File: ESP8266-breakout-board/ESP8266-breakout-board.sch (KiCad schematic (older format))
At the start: 3 parts, among them J1 Conn_01x04_Male, J2 Conn_02x04_Top_Bottom, J3 Conn_01x04_Male

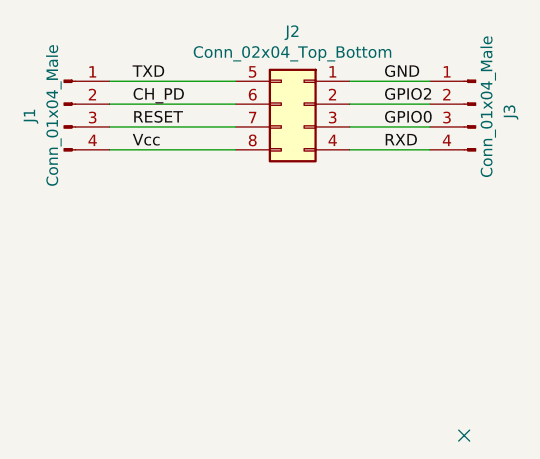
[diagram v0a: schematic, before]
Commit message: PCB esp8266-breakout-board
kicad-pcb with gerber files
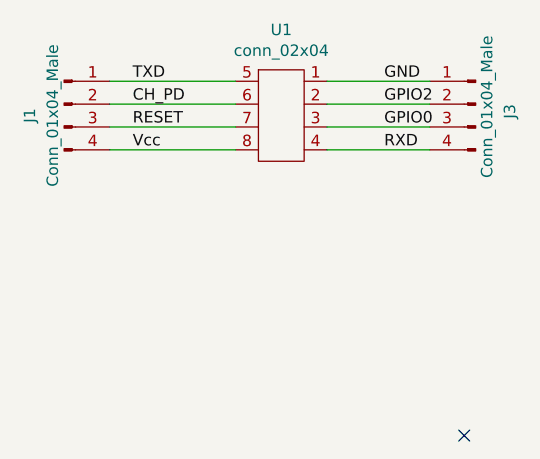
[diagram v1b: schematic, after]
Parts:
- removed J2: Conn_02x04_Top_Bottom, Connector_PinSocket_2.54mm:PinSocket_2x04_P2.54mm_Vertical, symbol Connector_Generic:Conn_02x04_Top_Bottom
- added U1: conn_02x04, conn_02x04:conn_02x04, symbol conn_02x04:conn_02x04
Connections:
- net CH_PD: now also U1.6
- net GND: now also U1.1
- net GPIO0: now also U1.3
- net GPIO2: now also U1.2
- net RESET: now also U1.7
- net RXD: now also U1.4
- net TXD: now also U1.5
- net Vcc: now also U1.8
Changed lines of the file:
@@
 NoConn ~ 5550 2550
 $Comp
-L Connector_Generic:Conn_02x04_Top_Bottom J2
-U 1 1 5F80BF5D
-P 4850 1100
-F 0 "J2" H 4900 1417 50  0000 C CNN
-F 1 "Conn_02x04_Top_Bottom" H 4900 1326 50  0000 C CNN
-F 2 "Connector_PinSocket_2.54mm:PinSocket_2x04_P2.54mm_Vertical" H 4850 1100 50  0001 C CNN
-F 3 "~" H 4850 1100 50  0001 C CNN
-	1    4850 1100
-	-1   0    0    -1
-$EndComp
-$Comp
 L Connector:Conn_01x04_Male J3
 U 1 1 5F80C5C2
@@
 $EndBitmap
 Wire Wire Line
-	5050 1000 5400 1000
-Wire Wire Line
-	5050 1100 5400 1100
-Wire Wire Line
-	5050 1200 5400 1200
-Wire Wire Line
-	5050 1300 5400 1300
-Wire Wire Line
 	4550 1000 4000 1000
 Wire Wire Line
@@
 Text Label 4100 1300 0    50   ~ 0
 Vcc
+$Comp
+L conn_02x04:conn_02x04 U1
+U 1 1 5F82EDFB
+P 4750 1050
+F 0 "U1" H 4750 1325 50  0000 C CNN
+F 1 "conn_02x04" H 4750 1234 50  0000 C CNN
+F 2 "conn_02x04:conn_02x04" H 4750 1050 50  0001 C CNN
+F 3 "" H 4750 1050 50  0001 C CNN
+	1    4750 1050
+	1    0    0    -1
+$EndComp
+Wire Wire Line
+	4950 1000 5400 1000
+Wire Wire Line
+	4950 1100 5400 1100
+Wire Wire Line
+	4950 1200 5400 1200
+Wire Wire Line
+	4950 1300 5400 1300
 $EndSCHEMATC
